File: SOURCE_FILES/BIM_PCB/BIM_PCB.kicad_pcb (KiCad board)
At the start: 4 copper layers, 63.5 x 72.5 mm, 209 parts, among them J1 Conn_02x02_Odd_Even, J2 Conn_02x03_Odd_Even, J3 Conn_01x06, J4 DISPLAY CONNECTOR, J5 nano_sim, J6 Conn_02x02_Odd_Even, Q1 SSM3J328R-HXY, Q10 2N7002, Q11 2N7002, Q2 SSM3J328R-HXY, Q3 IRLML0100TRPBF, Q4 BSN20, Q5 BSN20, Q6 2N7002, Q7 2N7002, Q8 2N7002, Q9 2N7002, SW1 reset, U1 STM32F103C8Tx, U10 TBU-CA065-200-WH, U11 SSP3485U, U12 TBU-CA065-200-WH, U13 ATA6561-GAQW-N, U14 MC74HC4052A, U15 MC74HC4052A, U18 TBU-CA065-200-WH, U19 SSP3485U, U2 PCF8523TK, U20 TBU-CA065-200-WH, U3 SIM7000G, U4 TBU-CA065-200-WH, U5 SSP3485U, U6 TBU-CA065-200-WH, U7 ADP2504ACPZ-R7_3.3V_VERSION, U8 W25Q32JVSS, U9 ATA6561-GAQW-N, Y1 8MHz, Y2 32.678KHz, Y3 32.678KHz

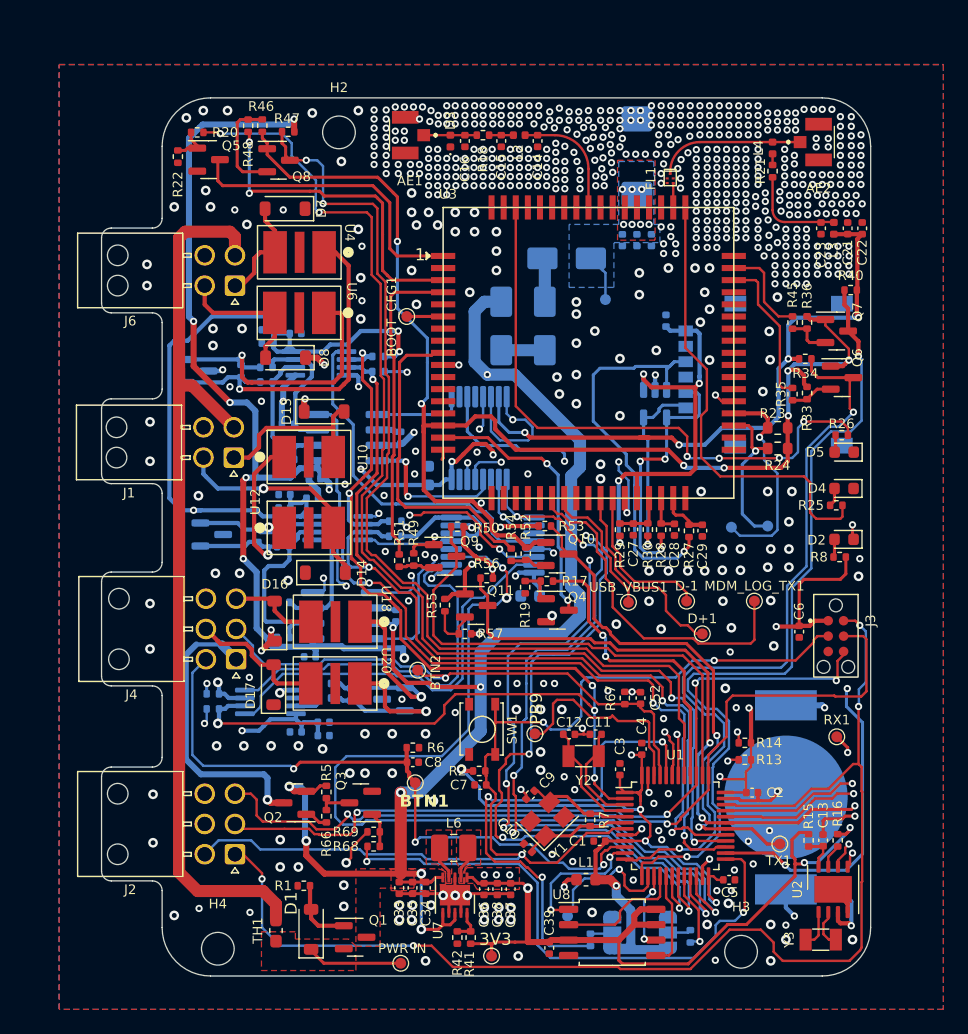
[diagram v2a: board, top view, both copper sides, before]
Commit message: updates on the buck 3v3 supply
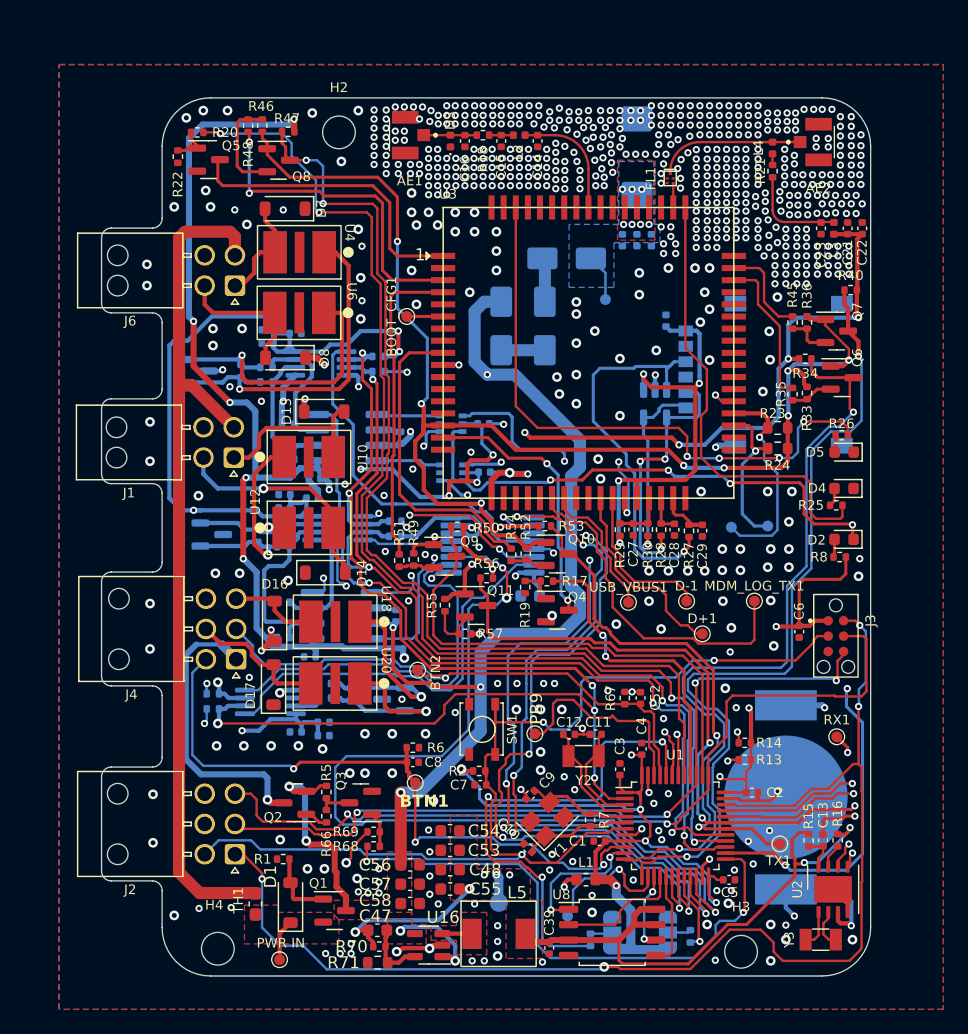
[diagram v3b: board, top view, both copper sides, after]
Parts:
- removed C35, C36, C38: 10u, Capacitor_SMD:C_0402_1005Metric
- removed C37: 100n, Capacitor_SMD:C_0402_1005Metric
- removed C45: 100n, Capacitor_SMD:C_0603_1608Metric
- removed L6: 1.5uH, Inductor_SMD:L_1008_2520Metric_Pad1.43x2.20mm_HandSolder
- removed R41: 0R, Resistor_SMD:R_0402_1005Metric
- removed R42: 1K, Resistor_SMD:R_0402_1005Metric
- removed TP6: TestPoint, brilliant-kicad-library:TestPoint_Pad_D0.9mm
- added C47: 8.2p, Capacitor_SMD:C_0603_1608Metric, F.Cu at (53.8, 126.5)
- added C48: 10n, Capacitor_SMD:C_0603_1608Metric, F.Cu at (59.8, 121.5)
- added C53: 33p, Capacitor_SMD:C_0603_1608Metric, F.Cu at (59.8, 119.9)
- added C54: 10p, Capacitor_SMD:C_0603_1608Metric, F.Cu at (59.8, 118.3)
- added C55: 22u, Capacitor_SMD:C_0603_1608Metric, F.Cu at (59.8, 123.1)
- added C56: 10u, Capacitor_SMD:C_0603_1608Metric, F.Cu at (56.5, 121.1)
- added C57: 10u, Capacitor_SMD:C_0603_1608Metric, F.Cu at (56.5, 122.7)
- added C58: 100n, Capacitor_SMD:C_0603_1608Metric, F.Cu at (56.5, 124.3)
- added L5: 2.2u, greencharge-footprints:MDA5030-100M, F.Cu at (61.6, 126.8)
- added R70: 180K, Resistor_SMD:R_0402_1005Metric, F.Cu at (53.9, 127.8)
- added R71: 40K, Resistor_SMD:R_0603_1608Metric, F.Cu at (53.8, 129.2)
- added TP9: TestPoint, TestPoint:TestPoint_Pad_D1.5mm, B.Cu at (63.8, 124.2)
- added U16: SY8089AAAC, Package_TO_SOT_SMD:SOT-23-5, F.Cu at (58.0, 127.7)
- C33: value 10u -> 100n; moved to B.Cu
- C34: moved to B.Cu
- U14: value MC74HC4052A -> WAS3157B; footprint Package_SO:SSOP-16_5.3x6.2mm_P0.65mm -> Package_TO_SOT_SMD:SOT-363_SC-70-6
- U7: value ADP2504ACPZ-R7_3.3V_VERSION -> WAS3157B; footprint Package_DFN_QFN:DFN-10-1EP_3x3mm_P0.5mm_EP1.7x2.5mm -> Package_TO_SOT_SMD:SOT-363_SC-70-6; moved to B.Cu
- moved C33 39.0 mm to (62.5, 84.7), turned to 0 degrees
- moved U7 38.9 mm to (59.9, 84.7), turned to 0 degrees
- moved C34 34.7 mm to (62.6, 88.7), turned to 0 degrees
- moved TP1 10.0 mm to (45.7, 128.9)
- moved U14 3.66 mm to (59.9, 88.7), turned to 0 degrees
- moved Q1 2.78 mm to (50.2, 124.8)
- moved R1 2.78 mm to (46.0, 120.6)
- moved D1 2.78 mm to (46.6, 124.2)
- moved TH1 2.78 mm to (43.7, 124.3)
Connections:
- C33 pad 1: +5V -> +3V3
- C34 pad 1: +5V -> +3V3
- D2 pad 1: /STM32FC8T6_MCU/SEL -> /MULTIPLEXER_SWITCH_WAS3157B-6/SEL
- U1 pad 26: /STM32FC8T6_MCU/SEL -> /MULTIPLEXER_SWITCH_WAS3157B-6/SEL
- U1 pad 32: /STM32FC8T6_MCU/CAN_RX -> /MULTIPLEXER_SWITCH_WAS3157B-6/SIG2_IN
- U1 pad 33: /STM32FC8T6_MCU/CAN_TX -> /MULTIPLEXER_SWITCH_WAS3157B-6/SIG1_IN
- U14 pad 1: /CAN_TX_2 -> /ecu_CAN_RX_2
- U14 pad 2: unconnected-(U14-Y2-Pad2) -> GND
- U14 pad 3: /STM32FC8T6_MCU/CAN_TX -> /CAN_RX_2
- U14 pad 4: unconnected-(U14-Y3-Pad4) -> /MULTIPLEXER_SWITCH_WAS3157B-6/SIG2_IN
- U14 pad 5: /ecu_CAN_TX_2 -> +3V3
- U14 pad 6: GND -> /MULTIPLEXER_SWITCH_WAS3157B-6/SEL
- U7 pad 1: +3V3 -> /ecu_CAN_TX_2
- U7 pad 2: Net-(U7-SW2) -> GND
- U7 pad 3: GND -> /CAN_TX_2
- U7 pad 4: Net-(U7-SW1) -> /MULTIPLEXER_SWITCH_WAS3157B-6/SIG1_IN
- U7 pad 5: +5V -> +3V3
- U7 pad 6: +5V -> /MULTIPLEXER_SWITCH_WAS3157B-6/SEL
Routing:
- net /MULTIPLEXER_SWITCH_WAS3157B-6/SEL: track 0.00 -> 90.8 mm, vias 0 -> 6
- net /STM32FC8T6_MCU/CAN_TX: track 68.4 -> 0.00 mm, vias 2 -> 0
- net /MULTIPLEXER_SWITCH_WAS3157B-6/SIG1_IN: track 0.00 -> 67.8 mm, vias 0 -> 2
- net /STM32FC8T6_MCU/CAN_RX: track 64.0 -> 0.00 mm, vias 2 -> 0
- net /MULTIPLEXER_SWITCH_WAS3157B-6/SIG2_IN: track 0.00 -> 63.8 mm, vias 0 -> 2
- net /STM32FC8T6_MCU/SEL: track 48.9 -> 0.00 mm, vias 3 -> 0
- net GND: track 92.3 -> 79.0 mm, vias 693 -> 702
- net +5V: track 125.5 -> 115.7 mm
- net /CAN_RX_2: track 12.6 -> 5.32 mm, vias 2 -> 0
- net Net-(U16-FB): track 0.00 -> 5.24 mm
- net Net-(D1-K): track 7.83 -> 3.42 mm
- net /MUX_SEL_B: track 63.3 -> 59.9 mm
- net VIN: track 76.7 -> 73.3 mm
- net /MUX_SEL_A: track 67.4 -> 64.1 mm
- net Net-(U7-SW1): track 2.75 -> 0.00 mm
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- removed copper zone on F.Cu, net Net-(U7-SW1)
- removed copper zone on F.Cu, net Net-(U7-SW2)

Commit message: update to A9G and connector
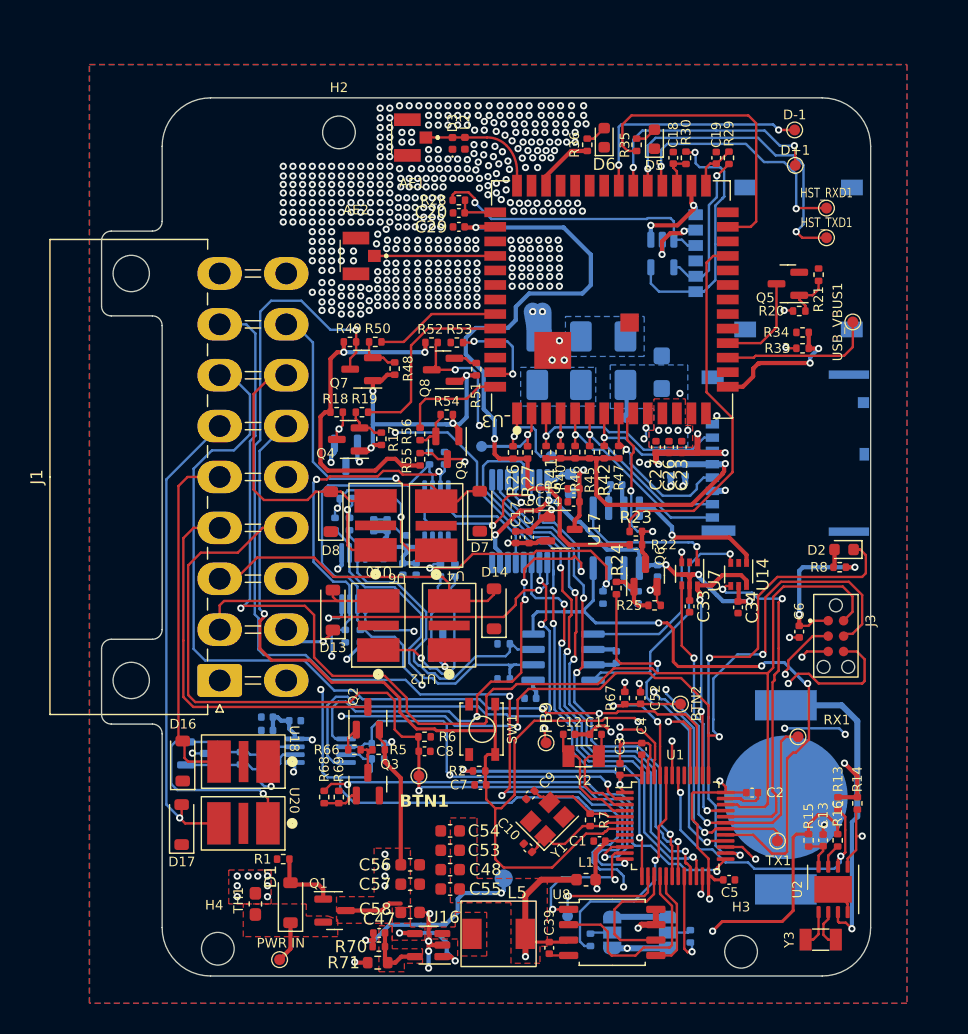
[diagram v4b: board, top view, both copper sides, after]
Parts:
- removed BOOT_CFG1: BOOT_CFG, brilliant-kicad-library:TestPoint_Pad_D0.9mm
- removed FL1: B39162B8813P810, Filter:Filter_1109-5_1.1x0.9mm
- removed J5: nano_sim, MACHADA_footprints:nano_sim_NSIM-2-C
- removed J6: Conn_02x02_Odd_Even, Connector_Molex:Molex_Nano-Fit_105314-xx04_2x02_P2.50mm_Horizontal
- removed L3: 100mHz 150/200R, Inductor_SMD:L_0402_1005Metric
- removed L4: 27nH, Inductor_SMD:L_0402_1005Metric
- removed MDM_LOG_TX1: MDM_LOG_TX, brilliant-kicad-library:TestPoint_Pad_D0.9mm
- removed Q10, Q11: 2N7002, Package_TO_SOT_SMD:SOT-23
- removed R57: 1K, Resistor_SMD:R_0402_1005Metric
- added HST_RXD1: HST_RXD, brilliant-kicad-library:TestPoint_Pad_D0.9mm, F.Cu at (90.8, 66.8)
- added HST_TXD1: HST_TXD, brilliant-kicad-library:TestPoint_Pad_D0.9mm, F.Cu at (90.8, 69.3)
- added R41: 10k, Resistor_SMD:R_0402_1005Metric, F.Cu at (67.7, 87.0)
- added R42: 10k, Resistor_SMD:R_0402_1005Metric, F.Cu at (72.5, 87.0)
- added U17: XC6206PxxxMR, Package_TO_SOT_SMD:SOT-23-3, F.Cu at (68.9, 93.4)
- C14: value 0.3p -> 0.1u
- C15: value ~ -> 1u
- C16: value ~ -> 0.1u
- C17, C33, C34, U14, U7: moved to F.Cu
- C18, C19: value 10u -> 22p; moved to F.Cu
- C20: value 1000u -> 22p; footprint Capacitor_Tantalum_SMD:CP_EIA-7343-43_Kemet-X -> Capacitor_SMD:C_0402_1005Metric; moved to F.Cu
- C21: value 1u -> 0.1u; moved to B.Cu
- C22: value 10n -> 1u; moved to B.Cu
- C23: value 1n -> 1u
- C26: value 100n -> 10u; moved to F.Cu
- C27: value 22p -> 10u
- C28: value 22p -> 100u; footprint Capacitor_SMD:C_0402_1005Metric -> Capacitor_Tantalum_SMD:CP_EIA-3216-18_Kemet-A; moved to B.Cu
- C29: value 22p -> 1u
- C47: footprint Capacitor_SMD:C_0603_1608Metric -> Capacitor_SMD:C_0402_1005Metric
- D4: value ORANGE -> SP0504BAHT; footprint LED_SMD:LED_0603_1608Metric -> Package_TO_SOT_SMD:SOT-23-5; moved to B.Cu
- D5: value BLUE -> ORANGE
- D6: value SP0504BAHT -> BLUE; footprint Package_TO_SOT_SMD:SOT-23-5 -> LED_SMD:LED_0603_1608Metric; moved to F.Cu
- J1: value Conn_02x02_Odd_Even -> Conn_02x09_Counter_Clockwise; footprint Connector_Molex:Molex_Nano-Fit_105314-xx04_2x02_P2.50mm_Horizontal -> Connector_Molex:Molex_Mini-Fit_Jr_5569-18A2_2x09_P4.20mm_Horizontal
- J2: value Conn_02x03_Odd_Even -> nano_sim; footprint Connector_Molex:Molex_Nano-Fit_105314-xx06_2x03_P2.50mm_Horizontal -> MACHADA_footprints:nano_sim_NSIM-2-C; moved to B.Cu
- J4: value DISPLAY CONNECTOR -> Micro_SD_Card; footprint Connector_Molex:Molex_Nano-Fit_105314-xx06_2x03_P2.50mm_Horizontal -> MACHADA_footprints:MOLEX_503398-1892; moved to B.Cu
- L2: value 1uH -> 82nH
- Q4: value BSN20 -> 2N7002
- Q6: value 2N7002 -> BSN20
- R17: value 1k -> 10K
- R18: value 0R -> 10K
- R19, R50, R53, R56: value 10K -> 1K
- R21: value 10R -> 10K
- R23, R24: value 2.2K -> 1k; footprint Resistor_SMD:R_0603_1608Metric -> Resistor_SMD:R_0402_1005Metric
- R25: value 390R -> 10K
- R26: value 390R -> 2.2K
- R27: value 22R -> 2.2K
- R29: value 10K -> 22R
- R33: value 10K -> 200K
- R34: value 10K -> 100K
- R35: value 1K -> 390R
- R36: value 10K -> 390R
- R40, R46, R47: value 10K -> 10k
- R45: value 1K -> 10k
- R48, R51, R54: value 1K -> 10K
- U3: value SIM7000G -> A9G_MODULE; footprint greencharge-footprints:SIM7000G -> MACHADA_footprints:A9G_MODULE
- moved J2 65.1 mm to (80.0, 67.4), turned to -90 degrees
- moved R20 51.8 mm to (88.6, 75.3), turned to 0 degrees
- moved R22 49.6 mm to (75.1, 94.7), turned to 180 degrees
- moved Q5 48.9 mm to (87.7, 73.1), turned to 180 degrees
- moved J4 48.1 mm to (87.1, 87.1), turned to -90 degrees
- moved D-1 39.9 mm to (88.2, 60.4)
- moved D+1 39.4 mm to (88.3, 63.3)
- moved Q7 39.4 mm to (52.5, 80.2), turned to 180 degrees
- moved AE2 39.3 mm to (52.0, 70.8), turned to 90 degrees
- moved R47 38.0 mm to (73.7, 87.0), turned to 90 degrees
- moved R46 37.3 mm to (70.1, 87.0)
- moved C16 33.1 mm to (66.3, 94.0)
- moved C29 32.1 mm to (60.5, 68.4), turned to 180 degrees
- moved R29 32.0 mm to (82.8, 62.7)
- moved R28 31.9 mm to (60.5, 66.2), turned to 180 degrees
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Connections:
- net /RS485_MAX486/B renamed /ECU_B
- C14 pad 1: GND -> 4.2V_SIMPWR
- C14 pad 2: Net-(U3-RF_ANT) -> GND
- C15 pad 1: GND -> 4.2V_SIMPWR
- C15 pad 2: Net-(C15-Pad2) -> GND
- C16 pad 1: GND -> 2V8
- C16 pad 2: Net-(AE1-A) -> GND
- C17 pad 1: 4.2V_SIMPWR -> 2V8
- C18 pad 1: 4.2V_SIMPWR -> /A9G_GSM_GPRS_MODULE/Sim_DIO
- C19 pad 1: 4.2V_SIMPWR -> /A9G_GSM_GPRS_MODULE/Sim_CLK
- C20 pad 1: 4.2V_SIMPWR -> /A9G_GSM_GPRS_MODULE/Sim_RST
- C21 pad 1: +3V3 -> /A9G_GSM_GPRS_MODULE/TF_CARD_CONN/2V8
- C22 pad 1: +3V3 -> /A9G_GSM_GPRS_MODULE/TF_CARD_CONN/2V8
- C23 pad 1: /SIM7000_GPRS_MODULE/gps_VDD -> 4.2V_SIMPWR
- C26 pad 1: /SIM7000_GPRS_MODULE/V_Sim -> 4.2V_SIMPWR
- C27 pad 1: /SIM7000_GPRS_MODULE/Sim_DIO -> 4.2V_SIMPWR
- C28 pad 1: /SIM7000_GPRS_MODULE/Sim_CLK -> 4.2V_SIMPWR
- C29 pad 1: /SIM7000_GPRS_MODULE/Sim_RST -> /A9G_GSM_GPRS_MODULE/VIO
- C7 pad 1: /STM32FC8T6_MCU/RESET -> /RESET
- D+1 pad 1: Net-(U3-USB_DP) -> Net-(U3-USB_P)
- D-1 pad 1: Net-(U3-USB_DM) -> Net-(U3-USB_N)
- D13 pad 2: /RS485_MAX486/A -> /ECU_A
- D16 pad 2: /RS485_MAX487/A -> /DIS_A
- D17 pad 2: /RS485_MAX487/B -> /DIS_B
- D2 pad 1: /MULTIPLEXER_SWITCH_WAS3157B-6/SEL -> Net-(D2-K)
- D4 pad 1: GND -> /A9G_GSM_GPRS_MODULE/V_Sim
- D4 pad 2: Net-(D4-A) -> GND
- D6 pad 1: /SIM7000_GPRS_MODULE/V_Sim -> GND
- D6 pad 2: GND -> Net-(D6-A)
- D7 pad 2: /RS485_MAX485/A -> /RS485_A
- D8 pad 2: /RS485_MAX485/B -> /RS485_B
- J1 pad 1: /RS485_MAX486/A -> VIN
- J1 pad 2: VIN -> /ECU_A
- J1 pad 4: GND -> Net-(J1-Pin_4)
- J3 pad 2: /STM32FC8T6_MCU/swdio -> /swdio
- J3 pad 3: /STM32FC8T6_MCU/RESET -> /RESET
- J3 pad 4: /STM32FC8T6_MCU/swdclk -> /swdclk
- J3 pad 6: /STM32FC8T6_MCU/SW0 -> /SW0
- J4 pad 1: Net-(J4-Pin_1) -> /A9G_GSM_GPRS_MODULE/TF_CARD_CONN/SD_D2
- J4 pad 2: /Button_2 -> /A9G_GSM_GPRS_MODULE/TF_CARD_CONN/SD_D3
- J4 pad 3: /RS485_MAX487/A -> /A9G_GSM_GPRS_MODULE/TF_CARD_CONN/SD_CMD
- J4 pad 4: /BUTTON -> /A9G_GSM_GPRS_MODULE/TF_CARD_CONN/2V8
- J4 pad 5: /RS485_MAX487/B -> /A9G_GSM_GPRS_MODULE/TF_CARD_CONN/SD_CLK
- L2 pad 1: Net-(U3-RF_ANT) -> GND
- L2 pad 2: Net-(C15-Pad2) -> Net-(AE1-A)
- Q2 pad 3: Net-(J4-Pin_1) -> Net-(J1-Pin_4)
- Q4 pad 1: Net-(Q4-G) -> 2V8
- Q4 pad 2: GND -> Net-(Q4-S)
- Q4 pad 3: /SIM7000_GPRS_MODULE/Reset -> /A9G_GSM_GPRS_MODULE/GPS_TXD
- Q6 pad 1: VDD_EXT -> Net-(Q6-G)
- Q6 pad 2: Net-(Q6-S) -> GND
- Q6 pad 3: /SIM7000_GPRS_MODULE/GPS_RXD -> Net-(Q6-D)
- Q7 pad 1: VDD_EXT -> 2V8
- Q7 pad 3: /SIM7000_GPRS_MODULE/GPS_TXD -> /A9G_GSM_GPRS_MODULE/GPS_RXD
- Q8 pad 1: VDD_EXT -> 2V8
- Q8 pad 3: /SIM7000_GPRS_MODULE/Sim_DTR -> /STM32FC8T6_MCU/TX1
- Q9 pad 1: VDD_EXT -> 2V8
- Q9 pad 3: /SIM7000_GPRS_MODULE/SIM_RI_(WAKE_HOST) -> /STM32FC8T6_MCU/RX1
- R17 pad 1: /SIM7000_GPRS_MODULE/Sim_Restart -> 2V8
- R17 pad 2: Net-(Q4-G) -> Net-(Q4-S)
- R18 pad 1: Net-(C15-Pad2) -> +3V3
- R18 pad 2: Net-(AE1-A) -> /A9G_GSM_GPRS_MODULE/GPS_TXD
- R19 pad 1: GND -> /A9G_GSM_GPRS_MODULE/MOSFET_LOGIC_LEVEL_TRANSLATOR6/LOW_SIDE_LOGIC_SIGNAL
- R19 pad 2: Net-(Q4-G) -> Net-(Q4-S)
- R2 pad 2: /STM32FC8T6_MCU/RESET -> /RESET
- R20 pad 1: /SIM7000_GPRS_MODULE/PWRKEY -> /A9G_GSM_GPRS_MODULE/Sim_Restart
- R21 pad 1: Net-(L4-Pad1) -> GND
- R21 pad 2: /SIM7000_GPRS_MODULE/gps_VDD -> Net-(Q5-G)
- R22 pad 1: GND -> Net-(Q6-D)
- R22 pad 2: Net-(Q5-G) -> /A9G_GSM_GPRS_MODULE/VIO
- R23 pad 1: Net-(U3-I2C_SCL) -> /A9G_GSM_GPRS_MODULE/IO29
- R23 pad 2: VDD_EXT -> Net-(Q6-D)
- R24 pad 1: Net-(U3-I2C_SDA) -> /A9G_GSM_GPRS_MODULE/PWRKEY
- R24 pad 2: VDD_EXT -> Net-(Q6-G)
- R25 pad 1: /SIM7000_GPRS_MODULE/NETLIGHT -> GND
- R25 pad 2: Net-(D4-A) -> Net-(Q6-G)
- R26 pad 1: /SIM7000_GPRS_MODULE/STATUS -> Net-(U3-I2C2_SCL/IO19)
- R26 pad 2: Net-(D5-A) -> /A9G_GSM_GPRS_MODULE/VIO
- R27 pad 1: /SIM7000_GPRS_MODULE/Sim_RST -> Net-(U3-I2C2_SDA/IO20)
- R27 pad 2: Net-(J5-RST) -> /A9G_GSM_GPRS_MODULE/VIO
- R28 pad 1: /SIM7000_GPRS_MODULE/Sim_CLK -> /A9G_GSM_GPRS_MODULE/Sim_RST
- R28 pad 2: Net-(J5-CLK) -> Net-(J2-RST)
- R29 pad 1: /SIM7000_GPRS_MODULE/Sim_DIO -> /A9G_GSM_GPRS_MODULE/Sim_CLK
- R29 pad 2: /SIM7000_GPRS_MODULE/V_Sim -> Net-(J2-CLK)
- R30 pad 1: /SIM7000_GPRS_MODULE/Sim_DIO -> /A9G_GSM_GPRS_MODULE/Sim_DIO
- R30 pad 2: Net-(J5-I/O) -> Net-(J2-I/O)
- R33 pad 1: VDD_EXT -> Net-(U3-ADC0)
- R33 pad 2: Net-(Q6-S) -> 4.2V_SIMPWR
- R34 pad 1: +3V3 -> GND
- R34 pad 2: /SIM7000_GPRS_MODULE/GPS_RXD -> Net-(U3-ADC0)
- R35 pad 1: /SIM7000_GPRS_MODULE/MOSFET_LOGIC_LEVEL_TRANSLATOR2/LOW_SIDE_LOGIC_SIGNAL -> /A9G_GSM_GPRS_MODULE/GPRS_NET-STATUS
- R35 pad 2: Net-(Q6-S) -> Net-(D5-A)
- R36 pad 1: VDD_EXT -> /A9G_GSM_GPRS_MODULE/GPS POSITION
- R36 pad 2: Net-(Q7-S) -> Net-(D6-A)
- R40 pad 1: +3V3 -> /A9G_GSM_GPRS_MODULE/TF_CARD_CONN/2V8
- R40 pad 2: /SIM7000_GPRS_MODULE/GPS_TXD -> /A9G_GSM_GPRS_MODULE/TF_CARD_CONN/SD_D2
- R45 pad 1: /SIM7000_GPRS_MODULE/MOSFET_LOGIC_LEVEL_TRANSLATOR3/LOW_SIDE_LOGIC_SIGNAL -> /A9G_GSM_GPRS_MODULE/TF_CARD_CONN/2V8
- R45 pad 2: Net-(Q7-S) -> /A9G_GSM_GPRS_MODULE/TF_CARD_CONN/SD_D0
- R46 pad 1: VDD_EXT -> /A9G_GSM_GPRS_MODULE/TF_CARD_CONN/2V8
- R46 pad 2: Net-(Q8-S) -> /A9G_GSM_GPRS_MODULE/TF_CARD_CONN/SD_D1
- R47 pad 1: +3V3 -> /A9G_GSM_GPRS_MODULE/TF_CARD_CONN/2V8
- R47 pad 2: /SIM7000_GPRS_MODULE/Sim_DTR -> /A9G_GSM_GPRS_MODULE/TF_CARD_CONN/SD_CLK
- R48 pad 1: /SIM7000_GPRS_MODULE/MOSFET_LOGIC_LEVEL_TRANSLATOR/LOW_SIDE_LOGIC_SIGNAL -> 2V8
- R48 pad 2: Net-(Q8-S) -> Net-(Q7-S)
- R49 pad 1: VDD_EXT -> +3V3
- R49 pad 2: Net-(Q9-S) -> /A9G_GSM_GPRS_MODULE/GPS_RXD
- R50 pad 1: +3V3 -> /A9G_GSM_GPRS_MODULE/MOSFET_LOGIC_LEVEL_TRANSLATOR7/LOW_SIDE_LOGIC_SIGNAL
- R50 pad 2: /SIM7000_GPRS_MODULE/SIM_RI_(WAKE_HOST) -> Net-(Q7-S)
- R51 pad 1: /SIM7000_GPRS_MODULE/MOSFET_LOGIC_LEVEL_TRANSLATOR5/LOW_SIDE_LOGIC_SIGNAL -> 2V8
- R51 pad 2: Net-(Q9-S) -> Net-(Q8-S)
- R52 pad 1: VDD_EXT -> +3V3
- R52 pad 2: Net-(Q10-S) -> /STM32FC8T6_MCU/TX1
- R53 pad 1: +3V3 -> /A9G_GSM_GPRS_MODULE/MOSFET_LOGIC_LEVEL_TRANSLATOR8/LOW_SIDE_LOGIC_SIGNAL
- R53 pad 2: /STM32FC8T6_MCU/TX1 -> Net-(Q8-S)
- R54 pad 1: /SIM7000_GPRS_MODULE/MOSFET_LOGIC_LEVEL_TRANSLATOR1/LOW_SIDE_LOGIC_SIGNAL -> 2V8
- R54 pad 2: Net-(Q10-S) -> Net-(Q9-S)
- R55 pad 1: VDD_EXT -> +3V3
- R55 pad 2: Net-(Q11-S) -> /STM32FC8T6_MCU/RX1
- R56 pad 1: +3V3 -> /A9G_GSM_GPRS_MODULE/MOSFET_LOGIC_LEVEL_TRANSLATOR9/LOW_SIDE_LOGIC_SIGNAL
- R56 pad 2: /STM32FC8T6_MCU/RX1 -> Net-(Q9-S)
- SIM_I2C_SCL1 pad 1: Net-(U3-I2C_SCL) -> Net-(U3-I2C2_SCL/IO19)
- SIM_I2C_SDA1 pad 1: Net-(U3-I2C_SDA) -> Net-(U3-I2C2_SDA/IO20)
- SW1 pad 2: /STM32FC8T6_MCU/RESET -> /RESET
- U1 pad 12: /SIM7000_GPRS_MODULE/GPS_RXD -> /A9G_GSM_GPRS_MODULE/GPS_RXD
- U1 pad 13: /SIM7000_GPRS_MODULE/GPS_TXD -> /A9G_GSM_GPRS_MODULE/GPS_TXD
- U1 pad 26: /MULTIPLEXER_SWITCH_WAS3157B-6/SEL -> Net-(D2-K)
- U1 pad 28: /SIM7000_GPRS_MODULE/PWRKEY -> /A9G_GSM_GPRS_MODULE/PWRKEY
- U1 pad 34: /STM32FC8T6_MCU/swdio -> /swdio
- U1 pad 37: /STM32FC8T6_MCU/swdclk -> /swdclk
- U1 pad 38: /SIM7000_GPRS_MODULE/SIM_RI_(WAKE_HOST) -> /MULTIPLEXER_SWITCH_WAS3157B-6/SEL
- U1 pad 39: /STM32FC8T6_MCU/SW0 -> /SW0
- U1 pad 40: /SIM7000_GPRS_MODULE/Sim_Restart -> /A9G_GSM_GPRS_MODULE/Sim_Restart
- U1 pad 41: /SIM7000_GPRS_MODULE/Sim_DTR -> /STM32FC8T6_MCU/Sim_DTR
- U1 pad 7: /STM32FC8T6_MCU/RESET -> /RESET
- U10 pad 2: /RS485_MAX486/A -> /ECU_A
- U18 pad 2: /RS485_MAX487/A -> /DIS_A
- U20 pad 2: /RS485_MAX487/B -> /DIS_B
- U4 pad 2: /RS485_MAX485/A -> /RS485_A
- U6 pad 2: /RS485_MAX485/B -> /RS485_B
- USB_VBUS1 pad 1: Net-(U3-USB_VBUS) -> Net-(U3-VUSB_DET)
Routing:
- net +3V3: track 274.0 -> 141.0 mm, vias 27 -> 12
- net VDD_EXT: track 126.9 -> 0.00 mm, vias 10 -> 0
- net /swdio: track 0.00 -> 110.7 mm, vias 0 -> 1
- net /RESET: track 0.00 -> 108.6 mm, vias 0 -> 3
- net /SW0: track 0.00 -> 106.8 mm, vias 0 -> 3
- net /STM32FC8T6_MCU/swdio: track 102.9 -> 0.00 mm, vias 4 -> 0
- net /SIM7000_GPRS_MODULE/PWRKEY: track 96.9 -> 0.00 mm, vias 4 -> 0
- net /A9G_GSM_GPRS_MODULE/GPS_RXD: track 0.00 -> 91.1 mm, vias 0 -> 4
- net /STM32FC8T6_MCU/RESET: track 87.7 -> 0.00 mm, vias 3 -> 0
- net /swdclk: track 0.00 -> 84.6 mm, vias 0 -> 4
- net /SIM7000_GPRS_MODULE/Sim_DTR: track 83.1 -> 0.00 mm, vias 2 -> 0
- net +3.3VA: track 112.7 -> 32.7 mm, vias 7 -> 3
- net VIN: track 73.3 -> 0.00 mm, vias 0 -> 8
- net /MULTIPLEXER_SWITCH_WAS3157B-6/SEL: track 90.8 -> 20.9 mm, vias 6 -> 2
- net /STM32FC8T6_MCU/swdclk: track 69.8 -> 0.00 mm, vias 2 -> 0
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- added copper zone on B.Cu, net Net-(D10-K)
- added copper zone on B.Cu, net Net-(D11-K)
- added copper zone on F.Cu, net Net-(U16-FB)
- added copper zone on F.Cu, net Net-(U16-LX)
- added copper zone on F.Cu, net VIN
- added copper zone on In2.Cu, net VIN
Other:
- outline, holes or cut-outs redrawn

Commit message: updated step
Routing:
- net GND: track 80.7 -> 142.2 mm, vias 475 -> 965
- net +3V3: track 141.0 -> 182.2 mm, vias 12 -> 17
- net +3.3VA: track 32.7 -> 60.4 mm, vias 3 -> 5
- net /CAN_TRANSCEIVER_ATA6562/A_to_CANL: track 5.47 -> 27.2 mm, vias 0 -> 2
- net +5V: track 92.9 -> 106.7 mm, vias 8 -> 9
- net /Button_2: track 69.9 -> 62.0 mm
- net Net-(Q8-S): track 1.96 -> 3.39 mm
- net Net-(U3-I2C2_SCL/IO19): track 8.42 -> 7.44 mm
- net /ecu_CAN_RX_2: track 11.5 -> 12.5 mm
- net /DISPLAY_RS485_RO: track 47.0 -> 46.2 mm
- net /RS485_A: track 28.7 -> 29.4 mm
- net /RS485_~{RE}: track 72.4 -> 73.1 mm
- net /RS485_RO: track 25.4 -> 26.0 mm
- net /ecu_RS485_RO: track 14.7 -> 14.2 mm
- net /RS485_DE: track 98.7 -> 99.2 mm

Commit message: updated GENERAL
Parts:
- moved TP9 2.57 mm to (66.2, 123.8)
- moved C22 0.19 mm to (79.0, 88.5)
- moved R51 0.19 mm to (61.8, 80.2)
- moved J4 0.19 mm to (86.9, 87.1)
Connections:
- Q8 pad 3: /STM32FC8T6_MCU/TX1 -> /STM32FC8T6_MCU/RX1
- Q9 pad 3: /STM32FC8T6_MCU/RX1 -> /STM32FC8T6_MCU/TX1
- R52 pad 2: /STM32FC8T6_MCU/TX1 -> /STM32FC8T6_MCU/RX1
- R55 pad 2: /STM32FC8T6_MCU/RX1 -> /STM32FC8T6_MCU/TX1
- U1 pad 12: /A9G_GSM_GPRS_MODULE/GPS_RXD -> /A9G_GSM_GPRS_MODULE/GPS_TXD
- U1 pad 13: /A9G_GSM_GPRS_MODULE/GPS_TXD -> /A9G_GSM_GPRS_MODULE/GPS_RXD
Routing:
- net /A9G_GSM_GPRS_MODULE/GPS_TXD: track 58.1 -> 98.1 mm
- net /A9G_GSM_GPRS_MODULE/GPS_RXD: track 91.1 -> 66.1 mm
- net +5V: track 106.7 -> 125.6 mm, vias 9 -> 11
- net GND: track 142.2 -> 155.6 mm, vias 965 -> 976
- net /STM32FC8T6_MCU/RX1: track 68.7 -> 79.1 mm, vias 3 -> 4
- net /STM32FC8T6_MCU/3v3_stm: track 104.6 -> 113.6 mm
- net /STM32FC8T6_MCU/TX1: track 70.5 -> 62.1 mm, vias 4 -> 3
- net Net-(U10-line_in): track 15.2 -> 17.6 mm
- net /swdclk: track 84.6 -> 82.9 mm
- net /RS485_DE: track 99.2 -> 97.8 mm
- net 2V8: track 41.9 -> 43.2 mm
- net /DISPLAY_PWR_EN: track 39.3 -> 40.5 mm
- net /CAN_TRANSCEIVER_ATA6561/A_to_CANL: track 29.6 -> 30.4 mm
- net /CAN_TRANSCEIVER_ATA6561/B_to_CANH: track 27.5 -> 28.3 mm
- net /CAN_STBY: track 54.8 -> 54.0 mm
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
